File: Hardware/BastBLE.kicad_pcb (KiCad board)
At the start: 2 copper layers, 50.8 x 22.9 mm, 39 parts, among them J1 Conn_Battery, J2 SWD, J3 Conn_left, J4 Conn_right, P1 USB_C_Plug_USB2.0, Q1 DMG3415U-7, SW1 RESET, U1 AP2112K-3.3, U2 E73-2G4M08S1C, U3 MCP73831-2-OT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

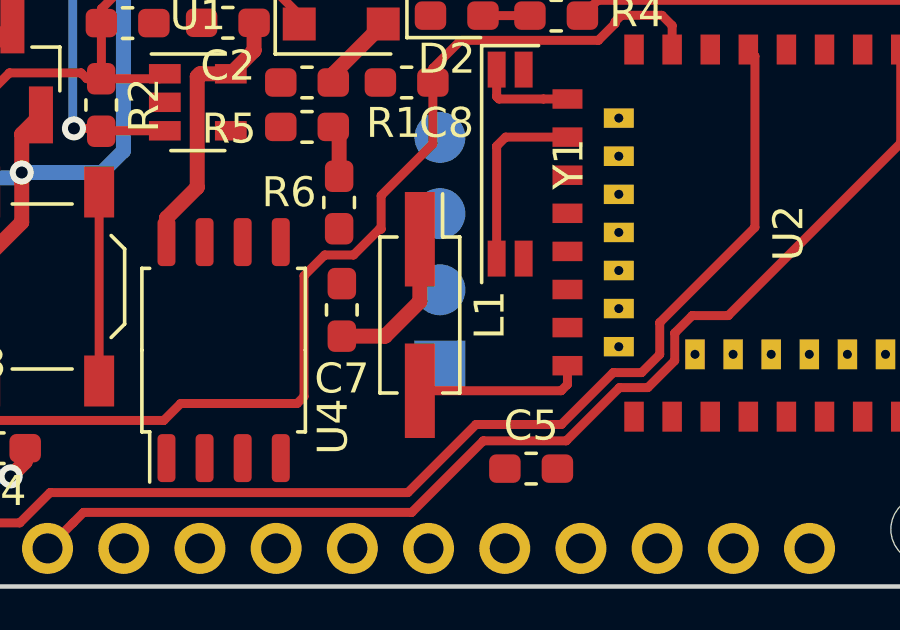
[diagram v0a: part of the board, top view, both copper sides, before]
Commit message: change L1 package
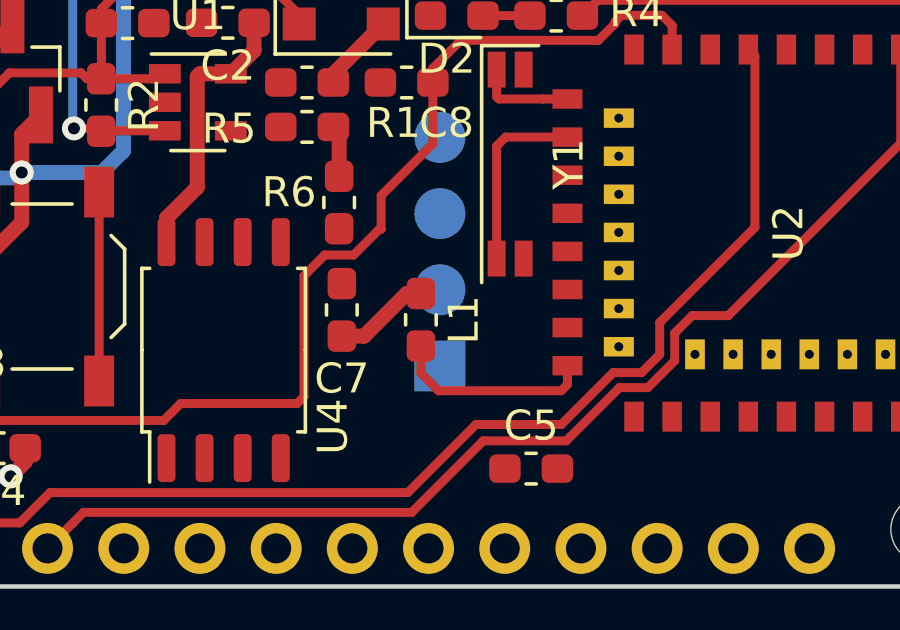
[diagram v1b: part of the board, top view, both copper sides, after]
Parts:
- L1: footprint Connector_PinHeader_2.54mm:PinHeader_2x01_P2.54mm_Vertical_SMD -> Inductor_SMD:L_0603_1608Metric_Pad1.05x0.95mm_HandSolder
- moved L1 0.16 mm to (158.5, 95.2)
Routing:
- net +3V3: track 29.6 -> 27.7 mm
- net Net-(L1-Pad2): track 5.63 -> 6.74 mm
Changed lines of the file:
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@@
-(kicad_pcb (version 20171130) (host pcbnew "(5.1.5)-3")
+(kicad_pcb (version 20171130) (host pcbnew "(5.1.5-0-10_14)")
   (general
     (thickness 1.6)
     (drawings 14)
-    (tracks 208)
+    (tracks 210)
     (zones 0)
     (modules 39)
@@
     (add_net VBUS)
   )
+  (module Inductor_SMD:L_0603_1608Metric_Pad1.05x0.95mm_HandSolder (layer F.Cu)
+    (at 158.496 95.25 270)
+    (descr "Capacitor SMD 0603 (1608 Metric), square (rectangular) end terminal, IPC_7351 nominal with elongated pad for handsoldering. (Body size source: http://www.tortai-tech.com/upload/download/2011102023233369053.pdf), generated with kicad-footprint-generator")
+    (tags "inductor handsolder")
+    (attr smd)
+    (fp_text reference L1 (at 0 -1.43 90) (layer F.SilkS)
+      (effects (font (size 1 1) (thickness 0.15)))
+    )
+    (fp_text value 10uH (at 0 1.43 90) (layer F.Fab)
+      (effects (font (size 1 1) (thickness 0.15)))
+    )
+    (fp_text user %R (at 0 0 90) (layer F.Fab)
+      (effects (font (size 0.4 0.4) (thickness 0.06)))
+    )
+    (fp_line (start 1.65 0.73) (end -1.65 0.73) (layer F.CrtYd) (width 0.05))
+    (fp_line (start 1.65 -0.73) (end 1.65 0.73) (layer F.CrtYd) (width 0.05))
+    (fp_line (start -1.65 -0.73) (end 1.65 -0.73) (layer F.CrtYd) (width 0.05))
+    (fp_line (start -1.65 0.73) (end -1.65 -0.73) (layer F.CrtYd) (width 0.05))
+    (fp_line (start -0.171267 0.51) (end 0.171267 0.51) (layer F.SilkS) (width 0.12))
+    (fp_line (start -0.171267 -0.51) (end 0.171267 -0.51) (layer F.SilkS) (width 0.12))
+    (fp_line (start 0.8 0.4) (end -0.8 0.4) (layer F.Fab) (width 0.1))
+    (fp_line (start 0.8 -0.4) (end 0.8 0.4) (layer F.Fab) (width 0.1))
+    (fp_line (start -0.8 -0.4) (end 0.8 -0.4) (layer F.Fab) (width 0.1))
+    (fp_line (start -0.8 0.4) (end -0.8 -0.4) (layer F.Fab) (width 0.1))
+    (pad 2 smd roundrect (at 0.875 0 270) (size 1.05 0.95) (layers F.Cu F.Paste F.Mask) (roundrect_rratio 0.25)
+      (net 47 "Net-(L1-Pad2)"))
+    (pad 1 smd roundrect (at -0.875 0 270) (size 1.05 0.95) (layers F.Cu F.Paste F.Mask) (roundrect_rratio 0.25)
+      (net 15 +3V3))
+    (model ${KISYS3DMOD}/Inductor_SMD.3dshapes/L_0603_1608Metric.wrl
+      (at (xyz 0 0 0))
+      (scale (xyz 1 1 1))
+      (rotate (xyz 0 0 0))
+    )
+  )
   (module Capacitor_SMD:C_0603_1608Metric_Pad1.05x0.95mm_HandSolder (layer F.Cu)
     (at 158.02 87.34 180)
@@
     )
   )
-  (module Connector_PinHeader_2.54mm:PinHeader_2x01_P2.54mm_Vertical_SMD (layer F.Cu)
-    (at 158.46 95.09 270)
-    (descr "surface-mounted straight pin header, 2x01, 2.54mm pitch, double rows")
-    (tags "Surface mounted pin header SMD 2x01 2.54mm double row")
-    (attr smd)
-    (fp_text reference L1 (at 0 -2.33 90) (layer F.SilkS)
-      (effects (font (size 1 1) (thickness 0.15)))
-    )
-    (fp_text value 10uH (at 0 2.33 90) (layer F.Fab)
-      (effects (font (size 1 1) (thickness 0.15)))
-    )
-    (fp_line (start 2.54 1.27) (end -2.54 1.27) (layer F.Fab) (width 0.1))
-    (fp_line (start -1.59 -1.27) (end 2.54 -1.27) (layer F.Fab) (width 0.1))
-    (fp_line (start -2.54 1.27) (end -2.54 -0.32) (layer F.Fab) (width 0.1))
-    (fp_line (start -2.54 -0.32) (end -1.59 -1.27) (layer F.Fab) (width 0.1))
-    (fp_line (start 2.54 -1.27) (end 2.54 1.27) (layer F.Fab) (width 0.1))
-    (fp_line (start -2.54 -0.32) (end -3.6 -0.32) (layer F.Fab) (width 0.1))
-    (fp_line (start -3.6 -0.32) (end -3.6 0.32) (layer F.Fab) (width 0.1))
-    (fp_line (start -3.6 0.32) (end -2.54 0.32) (layer F.Fab) (width 0.1))
-    (fp_line (start 2.54 -0.32) (end 3.6 -0.32) (layer F.Fab) (width 0.1))
-    (fp_line (start 3.6 -0.32) (end 3.6 0.32) (layer F.Fab) (width 0.1))
-    (fp_line (start 3.6 0.32) (end 2.54 0.32) (layer F.Fab) (width 0.1))
-    (fp_line (start -2.6 -1.33) (end 2.6 -1.33) (layer F.SilkS) (width 0.12))
-    (fp_line (start -2.6 1.33) (end 2.6 1.33) (layer F.SilkS) (width 0.12))
-    (fp_line (start -4.04 -0.76) (end -2.6 -0.76) (layer F.SilkS) (width 0.12))
-    (fp_line (start -2.6 -1.33) (end -2.6 -0.76) (layer F.SilkS) (width 0.12))
-    (fp_line (start 2.6 -1.33) (end 2.6 -0.76) (layer F.SilkS) (width 0.12))
-    (fp_line (start -2.6 0.76) (end -2.6 1.33) (layer F.SilkS) (width 0.12))
-    (fp_line (start 2.6 0.76) (end 2.6 1.33) (layer F.SilkS) (width 0.12))
-    (fp_line (start -5.9 -1.8) (end -5.9 1.8) (layer F.CrtYd) (width 0.05))
-    (fp_line (start -5.9 1.8) (end 5.9 1.8) (layer F.CrtYd) (width 0.05))
-    (fp_line (start 5.9 1.8) (end 5.9 -1.8) (layer F.CrtYd) (width 0.05))
-    (fp_line (start 5.9 -1.8) (end -5.9 -1.8) (layer F.CrtYd) (width 0.05))
-    (fp_text user %R (at 0 0) (layer F.Fab)
-      (effects (font (size 1 1) (thickness 0.15)))
-    )
-    (pad 1 smd rect (at -2.525 0 270) (size 3.15 1) (layers F.Cu F.Paste F.Mask)
-      (net 15 +3V3))
-    (pad 2 smd rect (at 2.525 0 270) (size 3.15 1) (layers F.Cu F.Paste F.Mask)
-      (net 47 "Net-(L1-Pad2)"))
-    (model ${KISYS3DMOD}/Connector_PinHeader_2.54mm.3dshapes/PinHeader_2x01_P2.54mm_Vertical_SMD.wrl
-      (at (xyz 0 0 0))
-      (scale (xyz 1 1 1))
-      (rotate (xyz 0 0 0))
-    )
-  )
   (module Button_Switch_SMD:SW_SPST_TL3342 (layer F.Cu)
     (at 145.87 94.14 90)
@@
   (segment (start 152.935 86.275) (end 152.16 87.05) (width 0.5) (layer F.Cu) (net 15))
   (segment (start 152.935 85.35) (end 152.935 86.275) (width 0.5) (layer F.Cu) (net 15))
-  (segment (start 158.46 94.64) (end 158.46 92.565) (width 0.5) (layer F.Cu) (net 15))
-  (segment (start 157.305 95.795) (end 158.46 94.64) (width 0.5) (layer F.Cu) (net 15))
-  (segment (start 155.86 95.795) (end 157.305 95.795) (width 0.5) (layer F.Cu) (net 15))
   (segment (start 150.015 91.86) (end 150.015 92.66) (width 0.5) (layer F.Cu) (net 15))
   (segment (start 151.040001 90.834999) (end 150.015 91.86) (width 0.5) (layer F.Cu) (net 15))
@@
   (segment (start 151.13 87.05) (end 151.040001 87.139999) (width 0.5) (layer F.Cu) (net 15))
   (segment (start 152.16 87.05) (end 151.13 87.05) (width 0.5) (layer F.Cu) (net 15))
+  (segment (start 156.601 95.795) (end 155.86 95.795) (width 0.5) (layer F.Cu) (net 15))
+  (segment (start 158.021 94.375) (end 156.601 95.795) (width 0.5) (layer F.Cu) (net 15))
+  (segment (start 158.496 94.375) (end 158.021 94.375) (width 0.5) (layer F.Cu) (net 15))
   (segment (start 147.855 88.95) (end 147.84 88.965) (width 0.3) (layer F.Cu) (net 18))
   (segment (start 149.96 88.95) (end 147.855 88.95) (width 0.3) (layer F.Cu) (net 18))
@@
   (segment (start 163.381 97.405) (end 163.381 96.78) (width 0.3) (layer F.Cu) (net 47))
   (segment (start 163.171 97.615) (end 163.381 97.405) (width 0.3) (layer F.Cu) (net 47))
-  (segment (start 158.46 97.615) (end 163.171 97.615) (width 0.3) (layer F.Cu) (net 47))
+  (segment (start 158.496 97.028) (end 158.496 96.125) (width 0.3) (layer F.Cu) (net 47))
+  (segment (start 159.083 97.615) (end 158.496 97.028) (width 0.3) (layer F.Cu) (net 47))
+  (segment (start 159.083 97.615) (end 163.171 97.615) (width 0.3) (layer F.Cu) (net 47))
 )

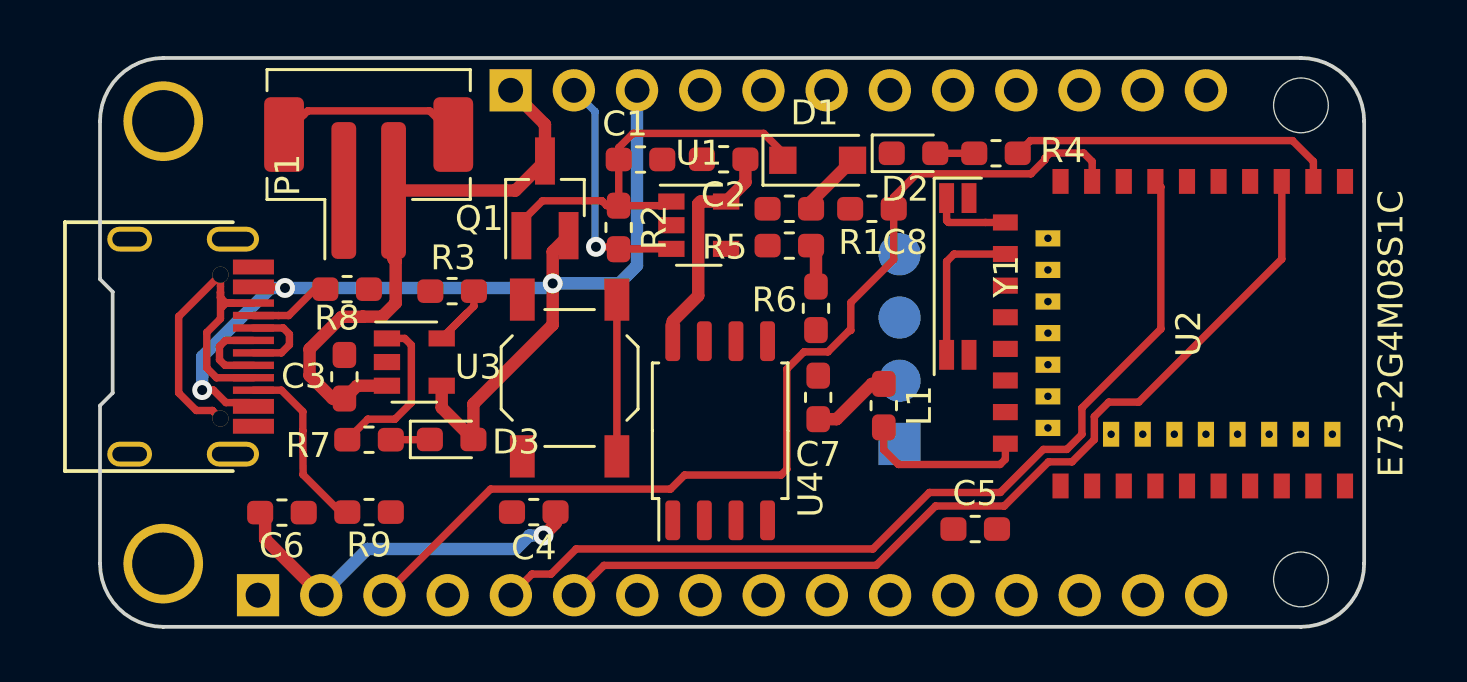
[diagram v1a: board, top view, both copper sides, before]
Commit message: fix failed components and tracks
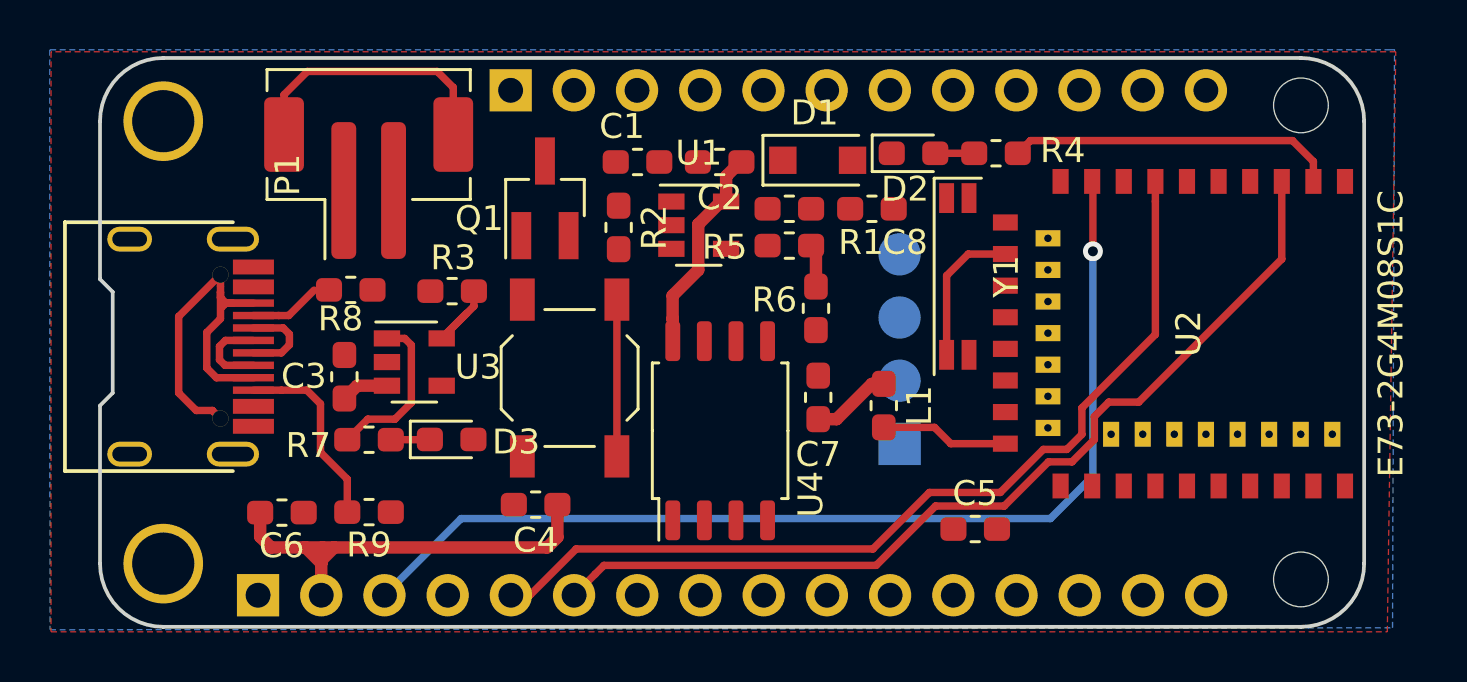
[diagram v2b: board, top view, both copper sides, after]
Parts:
- moved C4 0.31 mm to (144.5, 99.2)
- moved C2 0.19 mm to (151.9, 85.5)
- moved C1 0.16 mm to (148.6, 85.5)
- moved R8 0.15 mm to (137.1, 90.6)
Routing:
- net VBUS: track 46.1 -> 0.00 mm, vias 3 -> 0
- net +BATT: track 23.6 -> 1.92 mm
- net Net-(C1-Pad1): track 16.9 -> 0.00 mm
- net /EN: track 9.73 -> 0.00 mm, vias 1 -> 0
- net (no net): track 23.3 -> 26.7 mm
- net Net-(U2-Pad11): track 3.29 -> 0.00 mm
- net +3V3: track 27.7 -> 30.1 mm, vias 1 -> 0
- net Net-(L1-Pad2): track 6.74 -> 5.16 mm
- net /AREF: track 41.3 -> 42.3 mm, vias 0 -> 1
- added copper zone on B.Cu, net GND
- added copper zone on F.Cu, net GND

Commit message: routeo signals
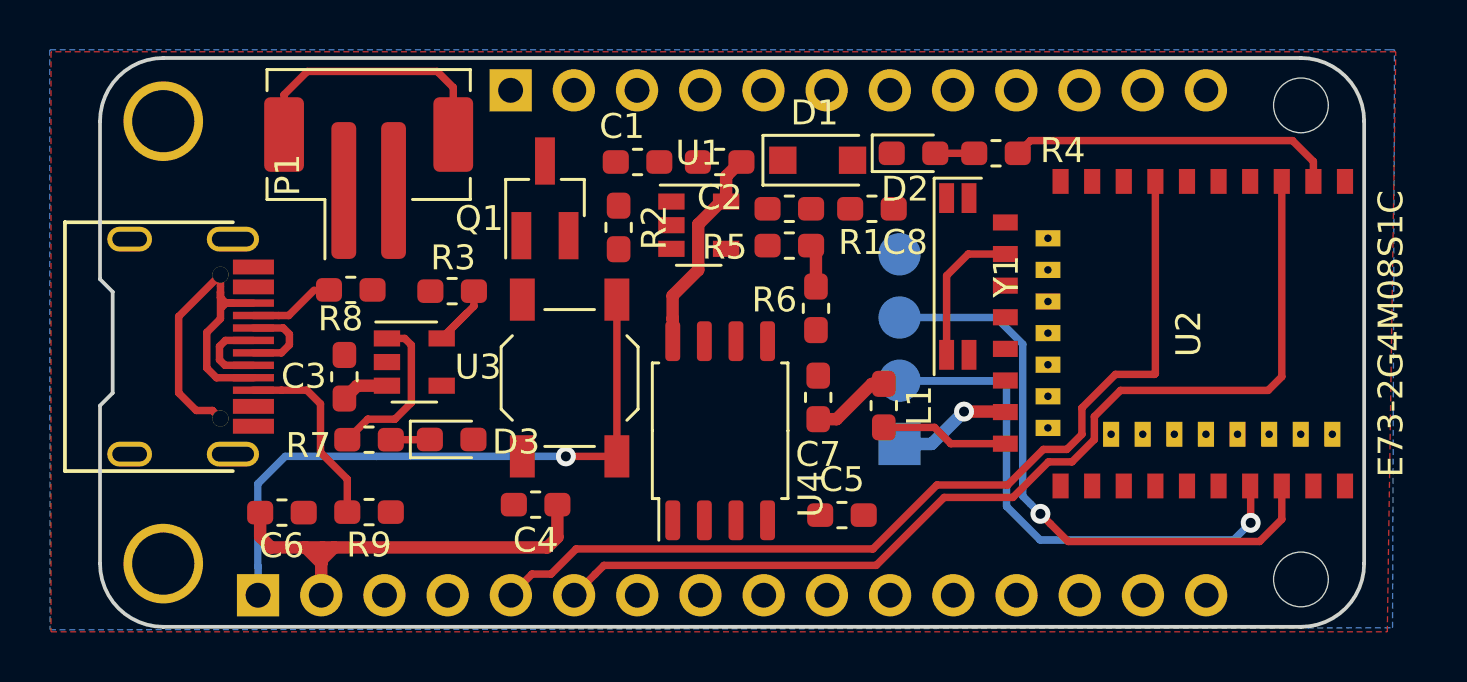
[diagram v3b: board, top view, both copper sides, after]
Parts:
- moved C5 5.38 mm to (156.8, 99.7)
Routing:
- net /AREF: track 42.3 -> 0.00 mm, vias 1 -> 0
- net /SWDIO: track 0.00 -> 25.2 mm, vias 0 -> 1
- net /SWCLK: track 0.00 -> 24.4 mm, vias 0 -> 1
- net /RST: track 6.30 -> 25.7 mm, vias 0 -> 1
- net +3V3: track 30.1 -> 34.9 mm, vias 0 -> 1
- net /A1: track 37.7 -> 40.5 mm
- net /A0: track 37.0 -> 37.9 mm

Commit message: Communication miso, mosi, tx, rx
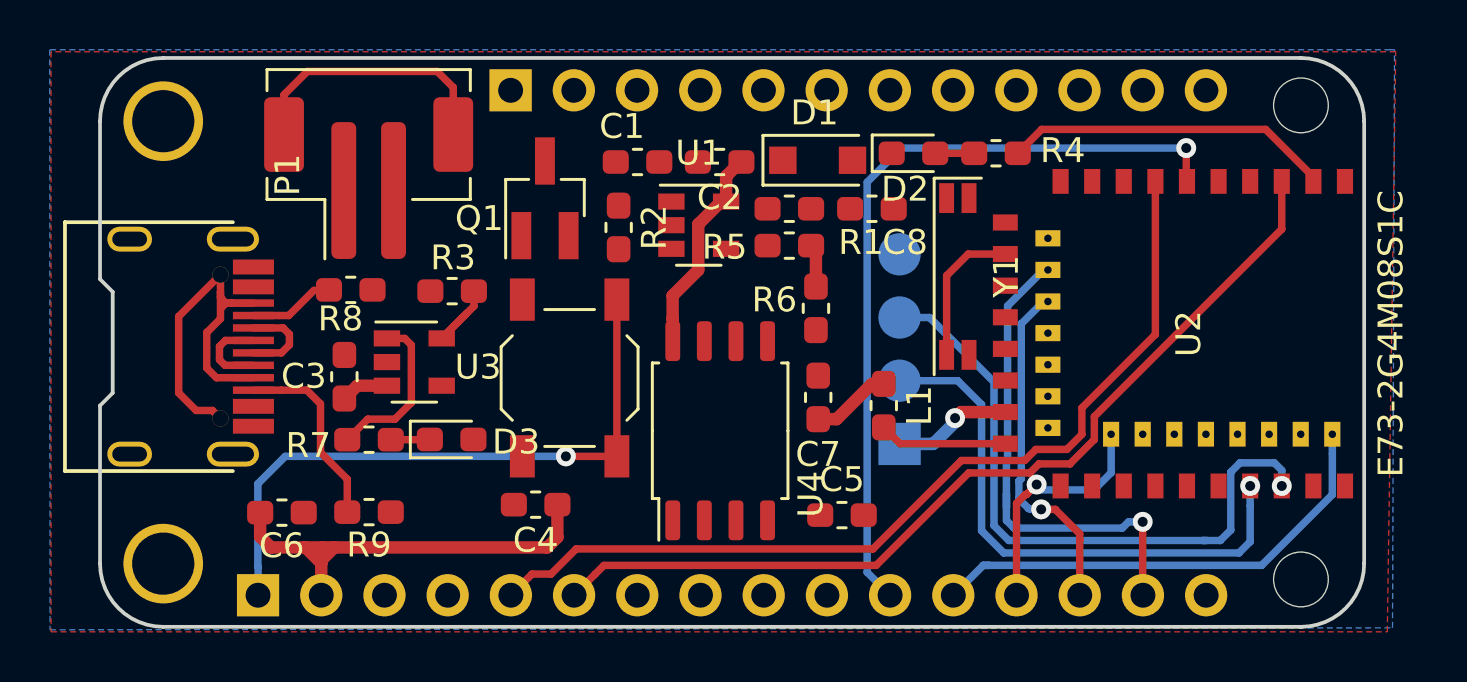
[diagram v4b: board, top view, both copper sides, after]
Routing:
- net /SCK: track 0.00 -> 31.7 mm, vias 0 -> 1
- net /TX: track 0.00 -> 20.1 mm, vias 0 -> 1
- net /MOSI: track 0.00 -> 19.6 mm
- net /RX: track 0.00 -> 14.1 mm, vias 0 -> 1
- net /MISO: track 0.00 -> 9.60 mm, vias 0 -> 1
- net /A1: track 40.5 -> 37.0 mm
- net /SWDIO: track 25.2 -> 22.4 mm
- net /SWCLK: track 24.4 -> 26.0 mm
- net /A0: track 37.9 -> 37.0 mm
